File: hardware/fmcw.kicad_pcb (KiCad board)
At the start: 4 copper layers, 147.8 x 58.9 mm, 414 parts, among them CON1 BARREL_JACK, J1 SD_Card, J2 USB_B_Micro, J3 SMA, J4 SMA, J5 SMA, P1 CONN_02X04, P2 CONN_02X04, Q1 DNP(RE1C002UN), Q2 RE1C002UN, SW1 SW_PUSH, U1 LP5907MFX-3.3, U10 LP5907MFX-3.0, U11 LTC2292, U12 ADF4158, U13 TLV172DCK, U14 PAT1220-3dB, U15 HMC431LP4, U16 PD4859J5050S2HF, U17 PAT1220-5dB, U18 SE5004L, U19 DC4759J5020AHF, U2 LP5907MFX-1.8, U20 PAT1220-6dB, U22 TRF37A73, U23 SKY65404, U24 TRF37A73, U25 SKY65404, U26 TPS5420D, U27 TPS5420D, U28 TPS560200, U29 LP2985A-10DBVR, U3 KT2520K-T, U30 TPS7A7001DDA, U31 TPS7A91, U32 TPS7A91, U33 LP5907MFX-3.0, U34 TPS7A91, U35 5400BL15B050E, U36 5400BL15B050E, U37 5400BL15B050E, U38 ADL5802, U39 ADA4940-2, U4 NC7SVU04P5X, U5 NB3N551, U6 XC7A15T-FTG256, U7 W25Q32JV, U8 93LCxxB, U9 FT2232H, Y1 12MHz

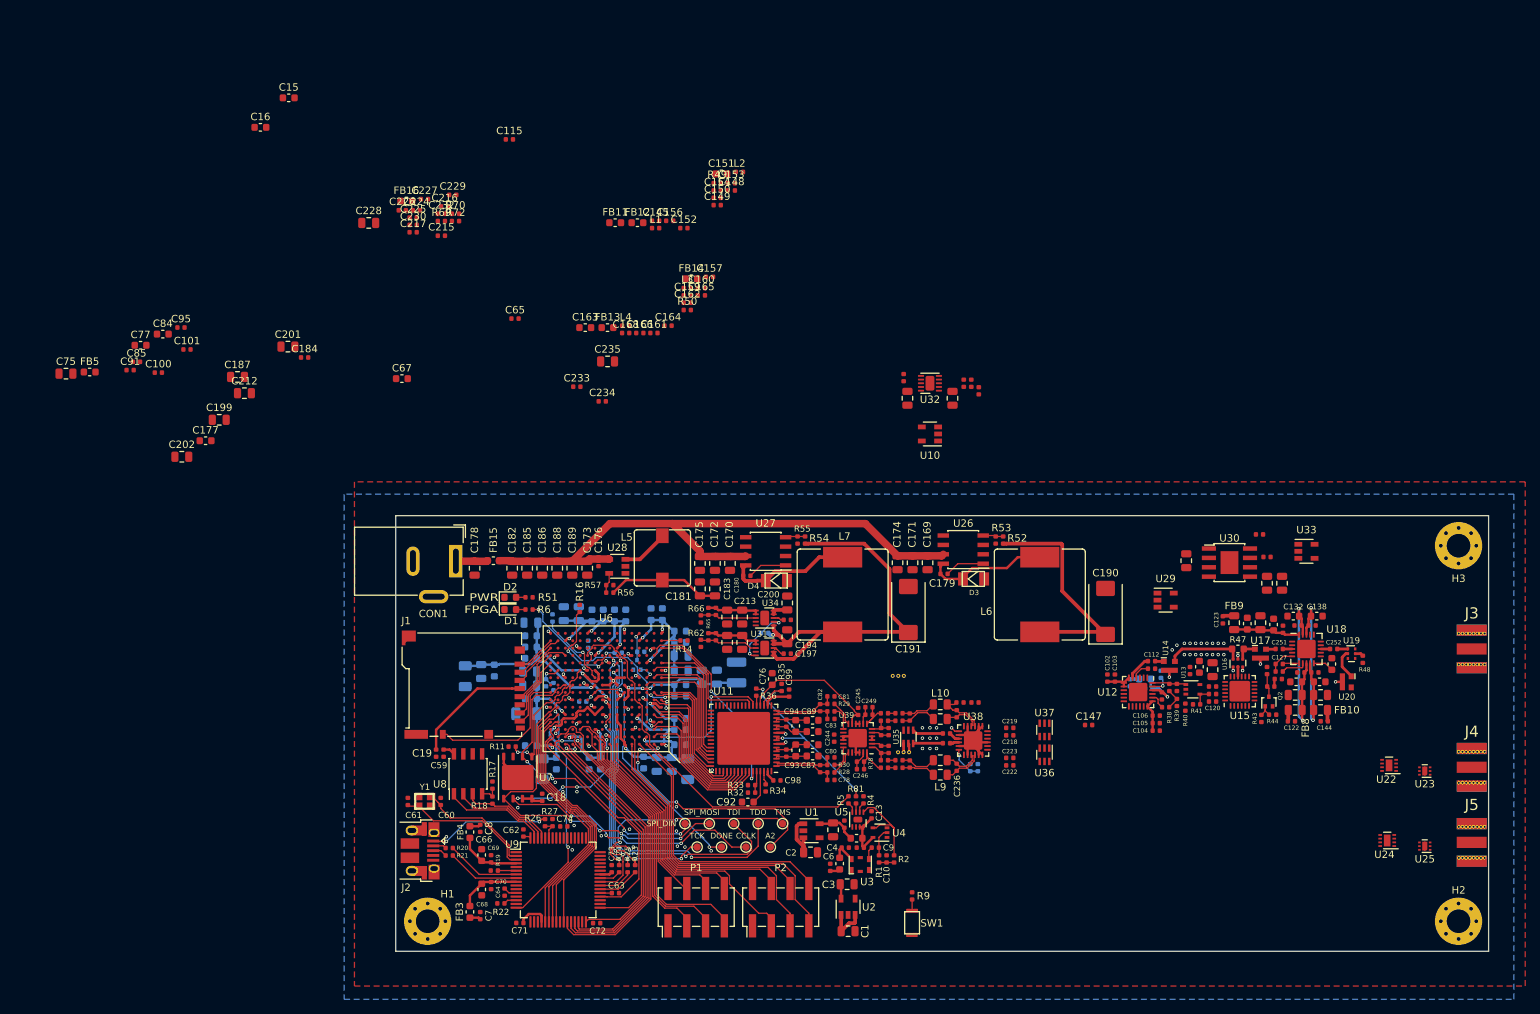
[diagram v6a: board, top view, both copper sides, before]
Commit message: Completed receivers.
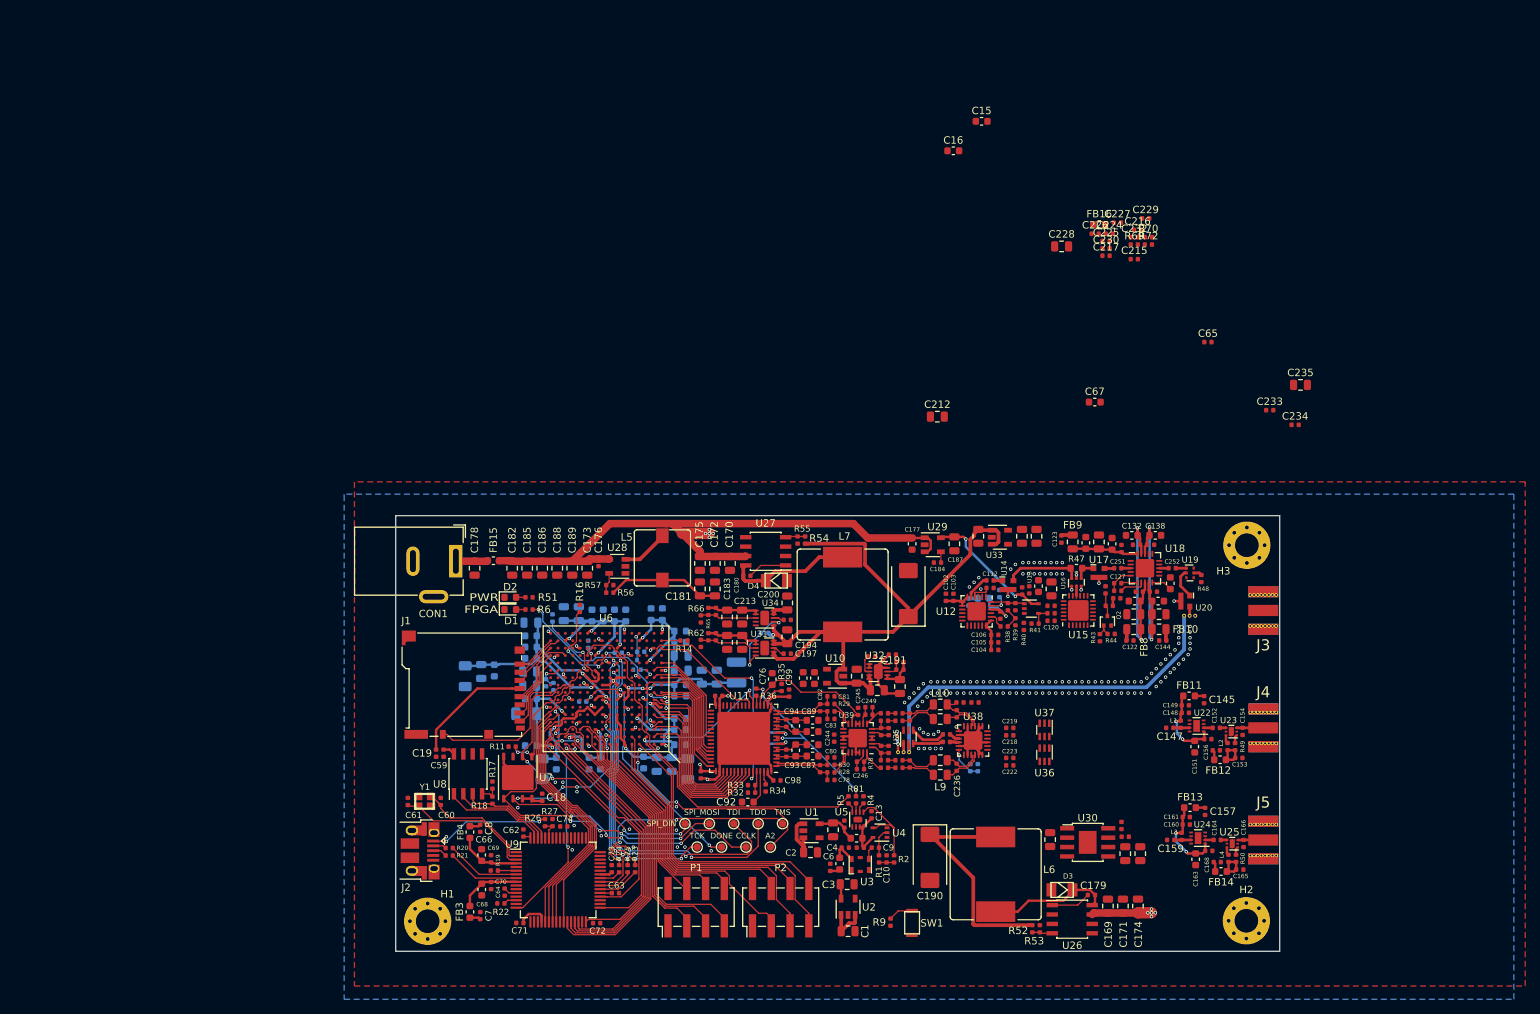
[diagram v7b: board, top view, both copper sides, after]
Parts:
- removed C85: 100n, Capacitor_SMD:C_0402_1005Metric
- removed FB5: BLM18PG181SH1D, Inductor_SMD:L_0603_1608Metric
- C91, C95: moved to B.Cu
- moved C202 116.1 mm to (173.0, 90.4), turned to 270 degrees
- moved C75 114.5 mm to (148.7, 109.3), turned to 90 degrees
- moved C163 109.5 mm to (194.6, 134.1), turned to 270 degrees
- moved L4 108.8 mm to (199.0, 134.0), turned to 270 degrees
- moved FB14 107.5 mm to (198.0, 135.8), turned to 180 degrees
- moved C168 107.4 mm to (197.5, 134.5)
- moved FB12 107.2 mm to (197.9, 120.7), turned to 180 degrees
- moved C166 106.9 mm to (201.0, 132.0), turned to 270 degrees
- moved C165 106.5 mm to (200.5, 135.5)
- moved R50 104.9 mm to (200.0, 134.0), turned to 270 degrees
- moved C199 103.9 mm to (165.2, 90.4), turned to 270 degrees
- moved C153 103.7 mm to (200.4, 120.4)
- moved R49 103.5 mm to (199.9, 118.9), turned to 270 degrees
- moved C156 102.9 mm to (197.4, 119.4)
- moved C201 102.6 mm to (171.1, 90.4), turned to 270 degrees
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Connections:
- net Net-(C220-Pad1) renamed /mixer/LOIb+
- net Net-(C220-Pad2) renamed /mixer/LOIa+
- net Net-(C221-Pad1) renamed /mixer/LOIb-
- net Net-(C221-Pad2) renamed /mixer/LOIa-
- C91 pad 1: Net-(C91-Pad1) -> Net-(C77-Pad1)
- C95 pad 1: Net-(C91-Pad1) -> Net-(C77-Pad1)
- C98 pad 1: Net-(C91-Pad1) -> Net-(C77-Pad1)
- C99 pad 1: Net-(C91-Pad1) -> Net-(C77-Pad1)
- U11 pad 10: Net-(C91-Pad1) -> Net-(C77-Pad1)
- U11 pad 18: Net-(C91-Pad1) -> Net-(C77-Pad1)
- U11 pad 63: Net-(C91-Pad1) -> Net-(C77-Pad1)
- U11 pad 7: Net-(C91-Pad1) -> Net-(C77-Pad1)
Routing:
- net /power/12V: track 81.4 -> 183.5 mm, vias 0 -> 10
- net GND: track 56.4 -> 148.9 mm, vias 77 -> 187
- net /LO: track 1.18 -> 54.3 mm
- net /3V6: track 73.1 -> 107.7 mm
- net /10V: track 0.00 -> 17.8 mm, vias 0 -> 2
- net Net-(C77-Pad1): track 0.00 -> 14.6 mm, vias 0 -> 2
- net Net-(C160-Pad1): track 0.00 -> 11.2 mm, vias 0 -> 2
- net Net-(C148-Pad1): track 0.00 -> 11.1 mm, vias 0 -> 2
- net Net-(C91-Pad1): track 7.95 -> 0.00 mm, vias 2 -> 0
- net /3V0: track 0.00 -> 5.22 mm
- net Net-(C165-Pad1): track 0.00 -> 4.82 mm
- net Net-(C153-Pad1): track 0.00 -> 4.82 mm
- net /3V3A: track 10.3 -> 15.2 mm
- net /3V3D: track 148.4 -> 152.8 mm
- net Net-(C154-Pad1): track 0.00 -> 3.60 mm
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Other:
- board size 147.8 x 58.9 mm -> 119.6 x 58.9 mm

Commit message: Finished placing.
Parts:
- moved C15 117.9 mm to (120.3, 143.1), turned to 90 degrees
- moved C16 106.2 mm to (144.8, 143.1), turned to 90 degrees
- moved C65 106.2 mm to (110.6, 127.0), turned to 270 degrees
- moved C67 88.4 mm to (111.9, 127.5), turned to 90 degrees
- moved R70 77.7 mm to (177.0, 126.9), turned to 90 degrees
- moved C229 76.3 mm to (178.1, 123.1), turned to 90 degrees
- moved C230 75.5 mm to (178.1, 126.9), turned to 270 degrees
- moved C233 73.1 mm to (145.7, 116.7), turned to 90 degrees
- moved R69 72.7 mm to (177.0, 123.1), turned to 90 degrees
- moved C235 72.0 mm to (155.6, 118.5), turned to 270 degrees
- moved C234 68.1 mm to (154.1, 116.9), turned to 90 degrees
- moved C227 67.8 mm to (180.2, 115.7), turned to 270 degrees
- moved C232 66.2 mm to (178.2, 115.7), turned to 270 degrees
- moved C226 66.2 mm to (181.2, 115.7), turned to 270 degrees
- moved C224 65.8 mm to (186.4, 115.2), turned to 180 degrees
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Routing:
- net /3V3D: track 152.8 -> 198.3 mm
- net /if/IF2a+: track 4.58 -> 21.0 mm
- net /if/IF2a-: track 4.88 -> 21.0 mm
- net /if/IF1a-: track 4.68 -> 20.1 mm
- net /if/IF1a+: track 4.98 -> 20.1 mm
- net /LO: track 54.3 -> 41.6 mm
- net GND: track 148.9 -> 136.2 mm, vias 187 -> 157
- net Net-(J3-Pad1): track 0.00 -> 11.1 mm
- net /RF2: track 0.00 -> 6.86 mm
- net /mixer/5VF: track 0.00 -> 6.68 mm
- net /RF1: track 0.00 -> 5.07 mm
- net /3V3A: track 15.2 -> 20.2 mm
- net /if/IF1+: track 4.71 -> 7.77 mm
- net /mixer/RF2b-: track 0.00 -> 3.04 mm
- net /fpga/usb/1V8: track 4.43 -> 7.47 mm
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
